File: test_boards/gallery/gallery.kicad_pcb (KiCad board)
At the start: 2 copper layers, 30 parts

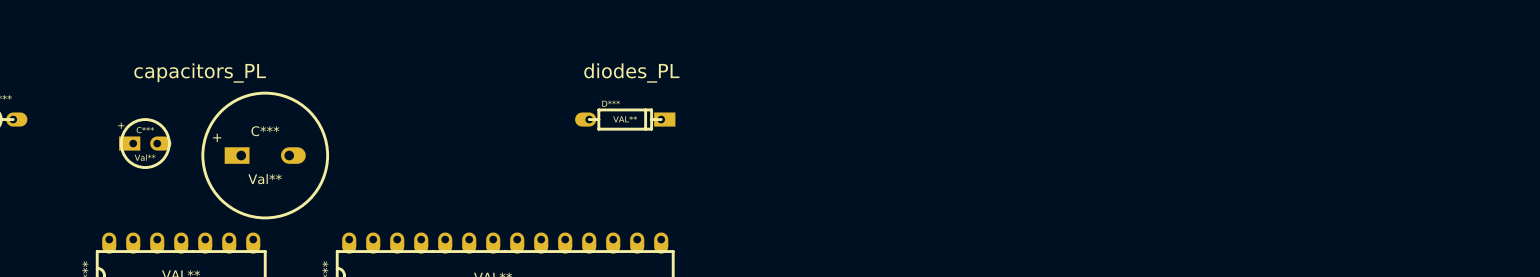
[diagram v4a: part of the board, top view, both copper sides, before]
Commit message: adding potentiometers
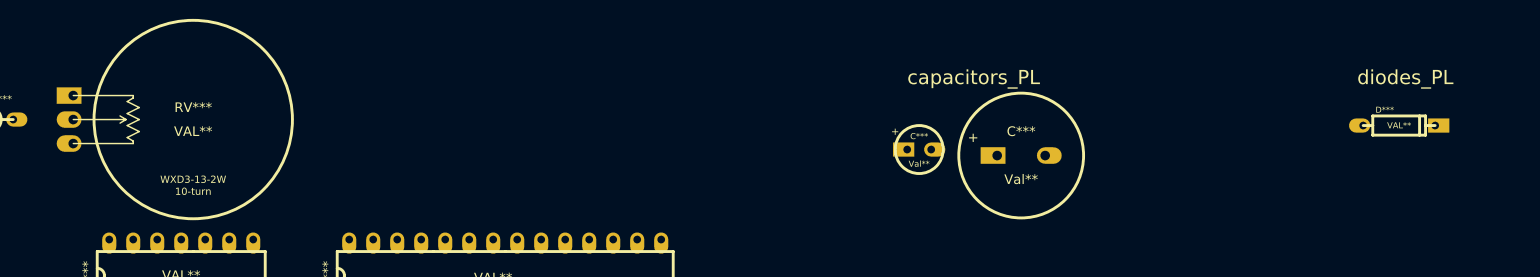
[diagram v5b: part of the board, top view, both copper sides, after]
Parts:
- added RV***: VAL**, WXD3-13-2W_A, F.Cu at (74.9, 22.9)
- moved C*** 81.9 mm to (150.5, 26.0)
- moved D*** 81.9 mm to (198.8, 23.5)
- moved C*** 80.0 mm to (160.0, 26.7)
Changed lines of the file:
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@@
     (tracks 22)
     (zones 0)
-    (modules 30)
+    (modules 31)
     (nets 1)
   )
@@
     (pcb_text_width 0.3)
     (pcb_text_size 1.5 1.5)
-    (mod_edge_width 0.3048)
+    (mod_edge_width 0.1524)
     (mod_text_size 1 1)
     (mod_text_width 0.15)
-    (pad_size 2.2479 1.4986)
-    (pad_drill 0.8128)
+    (pad_size 2.6289 1.7526)
+    (pad_drill 1.016)
     (pad_to_mask_clearance 0)
     (aux_axis_origin 0 0)
@@
   )
   (module ELCAP_10_20_V (layer F.Cu)
-    (at 68.58 25.4)
+    (at 150.495 26.035)
     (descr "Electrolytic Capacitor, vertical, 0.1\" pins, 0.2\" body")
     (tags CP)
@@
   )
   (module ELCAP_20_52_V (layer F.Cu)
-    (at 80.01 26.67)
+    (at 160.02 26.67)
     (descr "Electrolytic Capacitor, vertical, 0.2\" pins, 0.52\" body")
     (tags CP)
@@
   )
   (module DIODE_3 (layer F.Cu)
-    (at 116.84 22.86)
+    (at 198.755 23.495)
     (descr "Diode, 0.3\"")
     (tags "DIODE DEV")
@@
     )
   )
-  (gr_text diodes_PL (at 116.205 17.78) (layer F.SilkS)
+  (module WXD3-13-2W_A (layer F.Cu)
+    (at 74.93 22.86)
+    (descr "WXD3-13-2W 10-turn potentiometer (vertical, glued to PCB)")
+    (fp_text reference RV*** (at 0 -1.27) (layer F.SilkS)
+      (effects (font (size 1.016 1.016) (thickness 0.2032)))
+    )
+    (fp_text value VAL** (at 0 1.27) (layer F.SilkS)
+      (effects (font (size 1.016 1.016) (thickness 0.2032)))
+    )
+    (fp_line (start -7.112 0) (end -7.747 0.381) (layer F.SilkS) (width 0.1524))
+    (fp_line (start -7.112 0) (end -7.747 -0.381) (layer F.SilkS) (width 0.1524))
+    (fp_line (start -12.7 0) (end -7.112 0) (layer F.SilkS) (width 0.1524))
+    (fp_line (start -5.715 0) (end -6.985 0.635) (layer F.SilkS) (width 0.1524))
+    (fp_line (start -6.985 0.635) (end -5.715 1.27) (layer F.SilkS) (width 0.1524))
+    (fp_line (start -5.715 1.27) (end -6.985 1.905) (layer F.SilkS) (width 0.1524))
+    (fp_line (start -6.985 1.905) (end -6.35 2.286) (layer F.SilkS) (width 0.1524))
+    (fp_line (start -6.35 2.286) (end -6.35 2.54) (layer F.SilkS) (width 0.1524))
+    (fp_line (start -5.715 0) (end -6.985 -0.635) (layer F.SilkS) (width 0.1524))
+    (fp_line (start -6.985 -0.635) (end -5.715 -1.27) (layer F.SilkS) (width 0.1524))
+    (fp_line (start -5.715 -1.27) (end -6.985 -1.905) (layer F.SilkS) (width 0.1524))
+    (fp_line (start -6.985 -1.905) (end -6.35 -2.286) (layer F.SilkS) (width 0.1524))
+    (fp_line (start -6.35 -2.286) (end -6.35 -2.54) (layer F.SilkS) (width 0.1524))
+    (fp_line (start -12.7 2.54) (end -6.35 2.54) (layer F.SilkS) (width 0.1524))
+    (fp_line (start -12.7 -2.54) (end -6.35 -2.54) (layer F.SilkS) (width 0.1524))
+    (fp_text user 10-turn (at 0 7.62) (layer F.SilkS)
+      (effects (font (size 0.762 0.762) (thickness 0.1524)))
+    )
+    (fp_text user WXD3-13-2W (at 0 6.35) (layer F.SilkS)
+      (effects (font (size 0.762 0.762) (thickness 0.1524)))
+    )
+    (fp_circle (center 0 0) (end 10.5 0) (layer F.SilkS) (width 0.3048))
+    (pad 2 thru_hole oval (at -12.7 0) (size 2.6289 1.7526) (drill 1.016 (offset -0.43815 0))
+      (layers *.Cu *.Mask F.SilkS)
+    )
+    (pad 1 thru_hole rect (at -12.7 -2.54) (size 2.6289 1.7526) (drill 1.016 (offset -0.43815 0))
+      (layers *.Cu *.Mask F.SilkS)
+    )
+    (pad 3 thru_hole oval (at -12.7 2.54) (size 2.6289 1.7526) (drill 1.016 (offset -0.43815 0))
+      (layers *.Cu *.Mask F.SilkS)
+    )
+  )
+  (gr_text diodes_PL (at 198.12 18.415) (layer F.SilkS)
     (effects (font (size 1.5 1.5) (thickness 0.3)) (justify left))
   )
@@
     (effects (font (size 1.5 1.5) (thickness 0.3)) (justify left))
   )
-  (gr_text capacitors_PL (at 68.58 17.78) (layer F.SilkS)
+  (gr_text capacitors_PL (at 150.495 18.415) (layer F.SilkS)
     (effects (font (size 1.5 1.5) (thickness 0.3)) (justify left))
   )

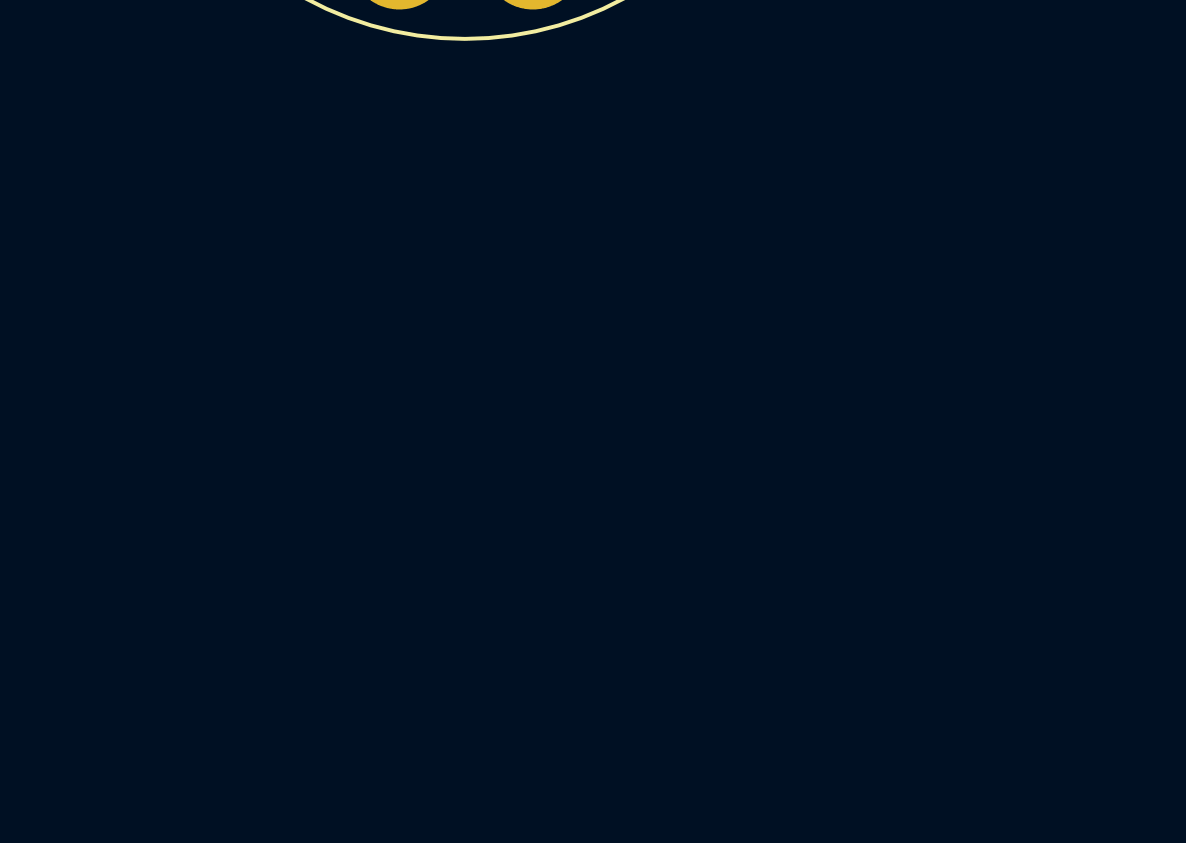
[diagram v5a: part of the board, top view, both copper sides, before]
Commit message: adding volt meter
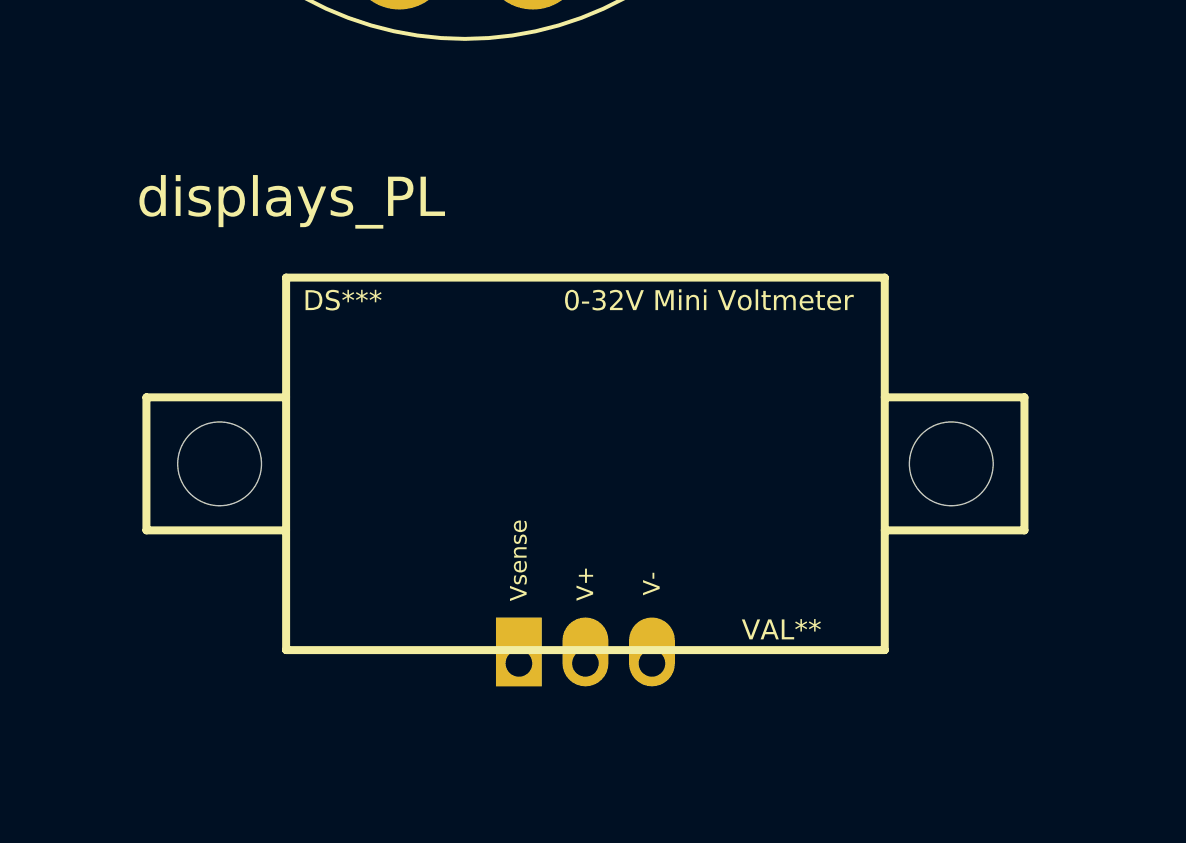
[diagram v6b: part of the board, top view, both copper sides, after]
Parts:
- added DS***: VAL**, DVM036A, F.Cu at (37.5, 207.0)
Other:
- board text added: "displays_PL"
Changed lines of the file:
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@@
     (links 0)
     (no_connects 0)
-    (area 17.030999 16.28 401.217201 279.357448)
+    (area 17.030999 11.953599 401.217201 279.357448)
     (thickness 1.6)
-    (drawings 11)
+    (drawings 12)
     (tracks 22)
     (zones 0)
-    (modules 31)
+    (modules 32)
     (nets 1)
   )
@@
     )
   )
+  (module DVM036A (layer F.Cu)
+    (at 37.465 207.01)
+    (descr "0-32V eBay Voltmeter")
+    (fp_text reference DS*** (at -9.271 -6.223) (layer F.SilkS)
+      (effects (font (size 0.762 0.762) (thickness 0.1524)))
+    )
+    (fp_text value VAL** (at 7.493 6.35) (layer F.SilkS)
+      (effects (font (size 0.762 0.762) (thickness 0.1524)))
+    )
+    (fp_text user V- (at 2.54 4.572 90) (layer F.SilkS)
+      (effects (font (size 0.635 0.635) (thickness 0.127)))
+    )
+    (fp_text user V+ (at 0 4.572 90) (layer F.SilkS)
+      (effects (font (size 0.635 0.635) (thickness 0.127)))
+    )
+    (fp_text user Vsense (at -2.54 3.683 90) (layer F.SilkS)
+      (effects (font (size 0.635 0.635) (thickness 0.127)))
+    )
+    (fp_text user "0-32V Mini Voltmeter" (at 4.699 -6.223) (layer F.SilkS)
+      (effects (font (size 0.762 0.762) (thickness 0.1524)))
+    )
+    (fp_line (start 11.43 -2.54) (end 16.764 -2.54) (layer F.SilkS) (width 0.3048))
+    (fp_line (start 16.764 -2.54) (end 16.764 2.54) (layer F.SilkS) (width 0.3048))
+    (fp_line (start 16.764 2.54) (end 11.43 2.54) (layer F.SilkS) (width 0.3048))
+    (fp_line (start -16.764 -2.54) (end -16.764 2.54) (layer F.SilkS) (width 0.3048))
+    (fp_line (start -16.764 2.54) (end -11.43 2.54) (layer F.SilkS) (width 0.3048))
+    (fp_line (start -16.764 -2.54) (end -11.43 -2.54) (layer F.SilkS) (width 0.3048))
+    (fp_line (start -11.43 -7.112) (end 11.43 -7.112) (layer F.SilkS) (width 0.3048))
+    (fp_line (start 11.43 -7.112) (end 11.43 7.112) (layer F.SilkS) (width 0.3048))
+    (fp_line (start 11.43 7.112) (end -11.43 7.112) (layer F.SilkS) (width 0.3048))
+    (fp_line (start -11.43 7.112) (end -11.43 -7.112) (layer F.SilkS) (width 0.3048))
+    (pad "" np_thru_hole circle (at -13.97 0) (size 3.2 3.2) (drill 3.2)
+      (layers *.Cu *.Mask F.SilkS)
+    )
+    (pad "" np_thru_hole circle (at 13.97 0) (size 3.2 3.2) (drill 3.2)
+      (layers *.Cu *.Mask F.SilkS)
+    )
+    (pad 1 thru_hole rect (at -2.54 7.62) (size 1.7526 2.6289) (drill 1.016 (offset 0 -0.43815))
+      (layers *.Cu *.Mask F.SilkS)
+    )
+    (pad 2 thru_hole oval (at 0 7.62) (size 1.7526 2.6289) (drill 1.016 (offset 0 -0.43815))
+      (layers *.Cu *.Mask F.SilkS)
+    )
+    (pad 3 thru_hole oval (at 2.54 7.62) (size 1.7526 2.6289) (drill 1.016 (offset 0 -0.43815))
+      (layers *.Cu *.Mask F.SilkS)
+    )
+  )
+  (gr_text displays_PL (at 20.32 196.85) (layer F.SilkS)
+    (effects (font (size 1.5 1.5) (thickness 0.3)) (justify left))
+  )
   (gr_text diodes_PL (at 198.12 18.415) (layer F.SilkS)

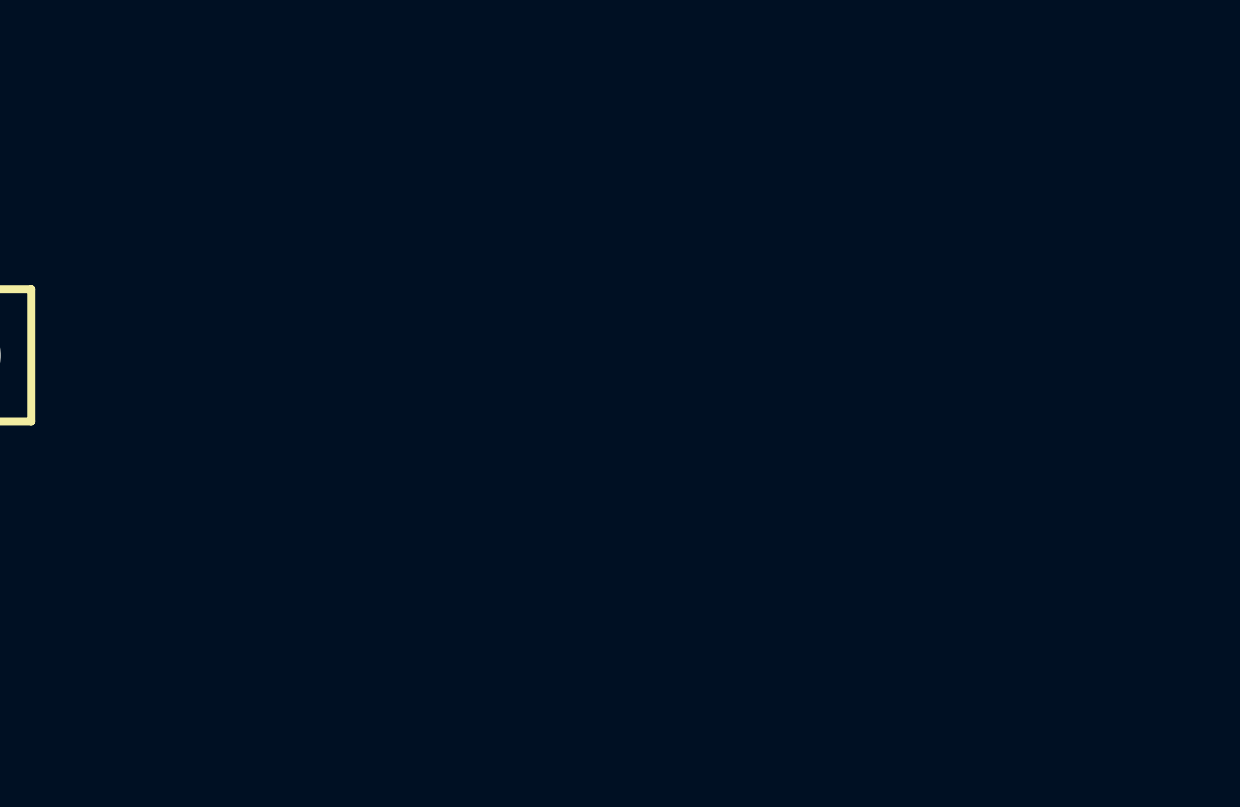
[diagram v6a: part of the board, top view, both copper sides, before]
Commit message: adding ebay ammeter footprint
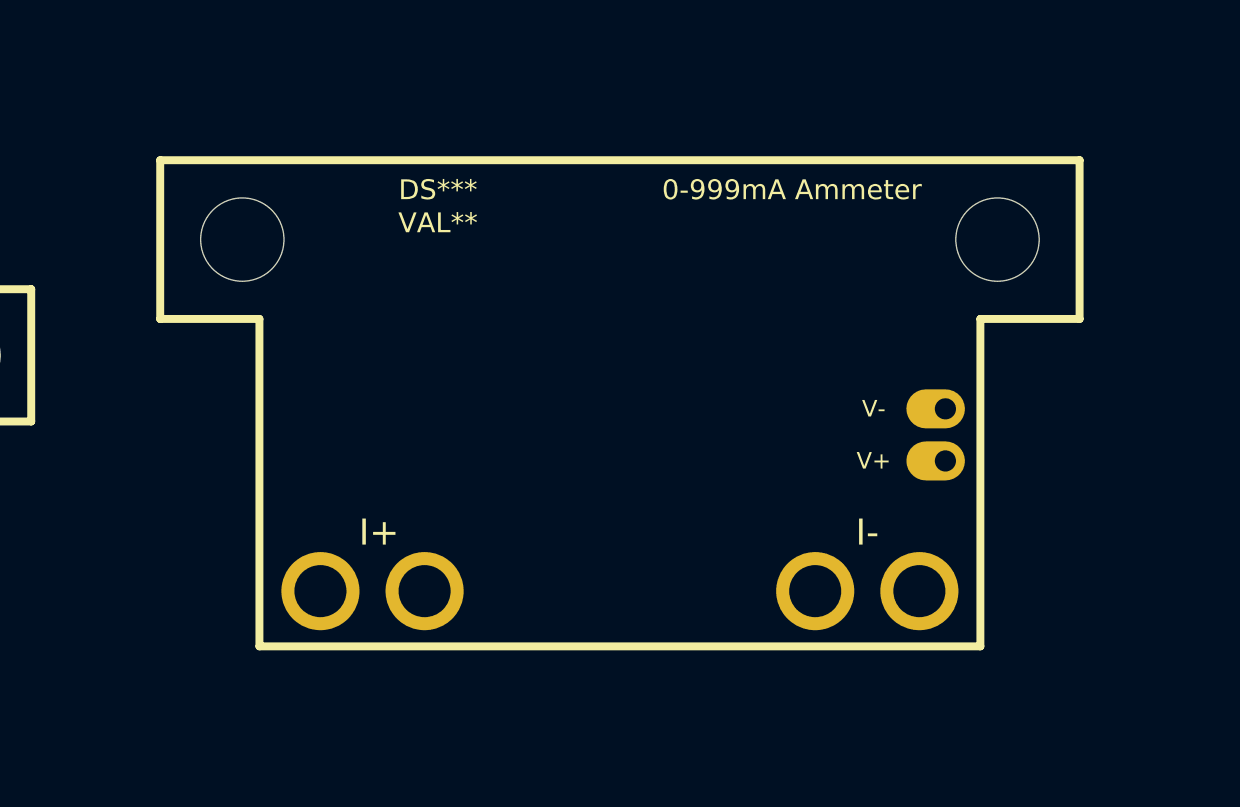
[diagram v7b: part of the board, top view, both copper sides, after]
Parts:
- added DS***: VAL**, EBAY_AMMETER, F.Cu at (76.8, 202.6)
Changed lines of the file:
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@@
     (tracks 22)
     (zones 0)
-    (modules 32)
+    (modules 33)
     (nets 1)
   )
@@
     (pcb_text_width 0.3)
     (pcb_text_size 1.5 1.5)
-    (mod_edge_width 0.1524)
+    (mod_edge_width 0.3048)
     (mod_text_size 1 1)
     (mod_text_width 0.15)
-    (pad_size 2.6289 1.7526)
-    (pad_drill 1.016)
+    (pad_size 2.2479 1.4986)
+    (pad_drill 0.8128)
     (pad_to_mask_clearance 0)
     (aux_axis_origin 0 0)
@@
       (layers *.Cu *.Mask F.SilkS)
     )
+  )
+  (module EBAY_AMMETER (layer F.Cu)
+    (at 76.835 202.565)
+    (descr "0-999mA eBay Ammeter")
+    (fp_text reference DS*** (at -6.985 -1.905) (layer F.SilkS)
+      (effects (font (size 0.762 0.762) (thickness 0.1524)))
+    )
+    (fp_text value VAL** (at -6.985 -0.635) (layer F.SilkS)
+      (effects (font (size 0.762 0.762) (thickness 0.1524)))
+    )
+    (fp_text user I- (at 9.5 11.25) (layer F.SilkS)
+      (effects (font (size 1 1) (thickness 0.15)))
+    )
+    (fp_text user I+ (at -9.25 11.25) (layer F.SilkS)
+      (effects (font (size 1 1) (thickness 0.15)))
+    )
+    (fp_line (start -13.843 3.048) (end -13.843 15.621) (layer F.SilkS) (width 0.3048))
+    (fp_line (start -13.843 15.621) (end 13.843 15.621) (layer F.SilkS) (width 0.3048))
+    (fp_line (start 13.843 15.621) (end 13.843 3.048) (layer F.SilkS) (width 0.3048))
+    (fp_line (start 17.653 3.048) (end 13.843 3.048) (layer F.SilkS) (width 0.3048))
+    (fp_line (start -17.653 3.048) (end -13.843 3.048) (layer F.SilkS) (width 0.3048))
+    (fp_line (start 17.653 -3.048) (end -17.653 -3.048) (layer F.SilkS) (width 0.3048))
+    (fp_line (start 17.653 -3.048) (end 17.653 3.048) (layer F.SilkS) (width 0.3048))
+    (fp_line (start -17.653 -3.048) (end -17.653 3.048) (layer F.SilkS) (width 0.3048))
+    (fp_text user V- (at 9.75 6.5) (layer F.SilkS)
+      (effects (font (size 0.635 0.635) (thickness 0.127)))
+    )
+    (fp_text user V+ (at 9.75 8.5) (layer F.SilkS)
+      (effects (font (size 0.635 0.635) (thickness 0.127)))
+    )
+    (fp_text user "0-999mA Ammeter" (at 6.604 -1.905) (layer F.SilkS)
+      (effects (font (size 0.762 0.762) (thickness 0.1524)))
+    )
+    (pad "" np_thru_hole circle (at -14.5 0) (size 3.2 3.2) (drill 3.2)
+      (layers *.Cu *.Mask F.SilkS)
+    )
+    (pad "" np_thru_hole circle (at 14.5 0) (size 3.2 3.2) (drill 3.2)
+      (layers *.Cu *.Mask F.SilkS)
+    )
+    (pad 2 thru_hole oval (at 12.5 6.5) (size 2.2479 1.4986) (drill 0.8128 (offset -0.37465 0))
+      (layers *.Cu *.Mask F.SilkS)
+    )
+    (pad 1 thru_hole circle (at -11.5 13.5) (size 3 3) (drill 2)
+      (layers *.Cu *.Mask F.SilkS)
+    )
+    (pad 3 thru_hole oval (at 12.5 8.5) (size 2.2479 1.4986) (drill 0.8128 (offset -0.37465 0))
+      (layers *.Cu *.Mask F.SilkS)
+    )
+    (pad 2 thru_hole circle (at 11.5 13.5) (size 3 3) (drill 2)
+      (layers *.Cu *.Mask F.SilkS)
+    )
+    (pad 1 thru_hole circle (at -7.5 13.5) (size 3 3) (drill 2)
+      (layers *.Cu *.Mask F.SilkS)
+    )
+    (pad 2 thru_hole circle (at 7.5 13.5) (size 3 3) (drill 2)
+      (layers *.Cu *.Mask F.SilkS)
+    )
